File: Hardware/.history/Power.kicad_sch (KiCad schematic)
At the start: 24 parts, among them J1 Conn_01x02_Pin, J2 MP1584 Breakout, J6 Conn_01x06_Pin, J7 Conn_01x06_Pin, SW2 SW_SPDT, SW5 SW_SPDT

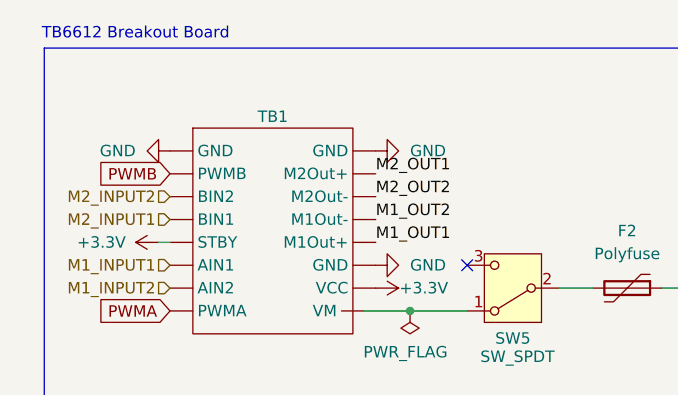
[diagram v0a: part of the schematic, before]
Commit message: Updated the ootprint of emitter and reciver to pinheader, largened the logo
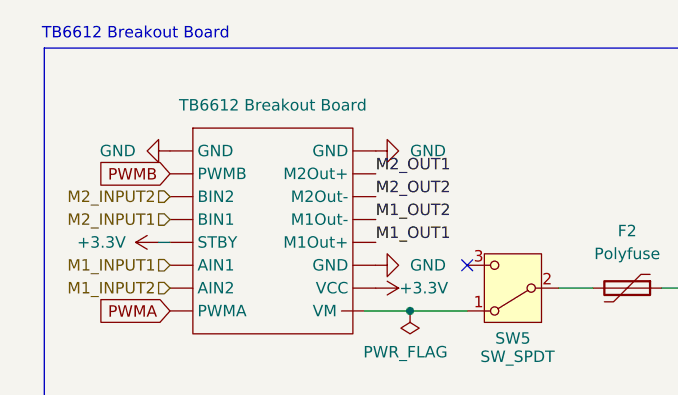
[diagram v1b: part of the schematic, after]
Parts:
- D3: footprint LED_THT:LED_D3.0mm -> Micromouse:LED_D3.0mm_micromouse
- TB1: value (none) -> TB6612 Breakout Board
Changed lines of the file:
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@@
-	)
-	(symbol
-		(lib_id "tb6612_module:TB6612_module")
-		(at 59.69 74.93 0)
-		(unit 1)
-		(body_style 1)
-		(exclude_from_sim no)
-		(in_bom yes)
-		(on_board yes)
-		(in_pos_files yes)
-		(dnp no)
-		(property "Reference" "TB1"
-			(at 66.04 68.58 0)
-			(show_name no)
-			(do_not_autoplace no)
-			(effects
-				(font
-					(size 1.27 1.27)
-				)
-			)
-		)
-		(property "Value" ""
-			(at 59.69 74.93 0)
-			(show_name no)
-			(do_not_autoplace no)
-			(effects
-				(font
-					(size 1.27 1.27)
-				)
-			)
-		)
-		(property "Footprint" "TB6612:TB6612 module"
-			(at 59.69 74.93 0)
-			(hide yes)
-			(show_name no)
-			(do_not_autoplace no)
-			(effects
-				(font
-					(size 1.27 1.27)
-				)
-			)
-		)
-		(property "Datasheet" ""
-			(at 59.69 74.93 0)
-			(hide yes)
-			(show_name no)
-			(do_not_autoplace no)
-			(effects
-				(font
-					(size 1.27 1.27)
-				)
-			)
-		)
-		(property "Description" ""
-			(at 59.69 74.93 0)
-			(hide yes)
-			(show_name no)
-			(do_not_autoplace no)
-			(effects
-				(font
-					(size 1.27 1.27)
-				)
-			)
-		)
-		(pin "1"
-		)
-		(pin "2"
-		)
-		(pin "3"
-		)
-		(pin "4"
-		)
-		(pin "9"
-		)
-		(pin "11"
-		)
-		(pin "16"
-		)
-		(pin "10"
-		)
-		(pin "5"
-		)
-		(pin "6"
-		)
-		(pin "8"
-		)
-		(pin "7"
-		)
-		(pin "12"
-		)
-		(pin "13"
-		)
-		(pin "14"
-		)
-		(pin "15"
-		)
-		(instances
-			(project "HSM_Project"
-				(path "/10a490ba-03bd-419b-97f3-e1946b38fc40/ac18e862-6ffc-44ea-b67e-4cb824815cfe"
-					(reference "TB1")
-					(unit 1)
-				)
-			)
-		)
 	)
 	(symbol
@@
 			)
 		)
-		(property "Footprint" "LED_THT:LED_D3.0mm"
+		(property "Footprint" "Micromouse:LED_D3.0mm_micromouse"
 			(at 130.81 120.65 0)
 			(hide yes)
@@
 					(unit 1)
 				)
+			)
+		)
+	)
+	(symbol
+		(lib_id "tb6612_module:TB6612_module")
+		(at 59.69 74.93 0)
+		(unit 1)
+		(body_style 1)
+		(exclude_from_sim no)
+		(in_bom yes)
+		(on_board yes)
+		(in_pos_files yes)
+		(dnp no)
+		(fields_autoplaced yes)
+		(property "Reference" "TB1"
+			(at 66.04 67.31 0)
+			(hide yes)
+			(show_name no)
+			(do_not_autoplace no)
+			(effects
+				(font
+					(size 1.27 1.27)
+				)
+			)
+		)
+		(property "Value" "TB6612 Breakout Board"
+			(at 66.04 67.31 0)
+			(show_name no)
+			(do_not_autoplace no)
+			(effects
+				(font
+					(size 1.27 1.27)
+				)
+			)
+		)
+		(property "Footprint" "TB6612:TB6612 module"
+			(at 59.69 74.93 0)
+			(hide yes)
+			(show_name no)
+			(do_not_autoplace no)
+			(effects
+				(font
+					(size 1.27 1.27)
+				)
+			)
+		)
+		(property "Datasheet" ""
+			(at 59.69 74.93 0)
+			(hide yes)
+			(show_name no)
+			(do_not_autoplace no)
+			(effects
+				(font
+					(size 1.27 1.27)
+				)
+			)
+		)
+		(property "Description" ""
+			(at 59.69 74.93 0)
+			(hide yes)
+			(show_name no)
+			(do_not_autoplace no)
+			(effects
+				(font
+					(size 1.27 1.27)
+				)
+			)
+		)
+		(pin "7"
+		)
+		(pin "2"
+		)
+		(pin "4"
+		)
+		(pin "6"
+		)
+		(pin "5"
+		)
+		(pin "11"
+		)
+		(pin "10"
+		)
+		(pin "1"
+		)
+		(pin "3"
+		)
+		(pin "9"
+		)
+		(pin "8"
+		)
+		(pin "13"
+		)
+		(pin "14"
+		)
+		(pin "15"
+		)
+		(pin "12"
+		)
+		(pin "16"
+		)
+		(instances
+			(project "HSM_Project"
+				(path "/10a490ba-03bd-419b-97f3-e1946b38fc40/ac18e862-6ffc-44ea-b67e-4cb824815cfe"
+					(reference "TB1")
+					(unit 1)
+				)
